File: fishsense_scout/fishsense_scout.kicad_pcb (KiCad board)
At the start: 2 copper layers, 19.5 x 22 mm, 21 parts, among them J1 Conn_01x02_Pin, J2 Conn_01x02_Pin, Q1 NPN, Q2 PMOS, U1 LMR16030PDDA

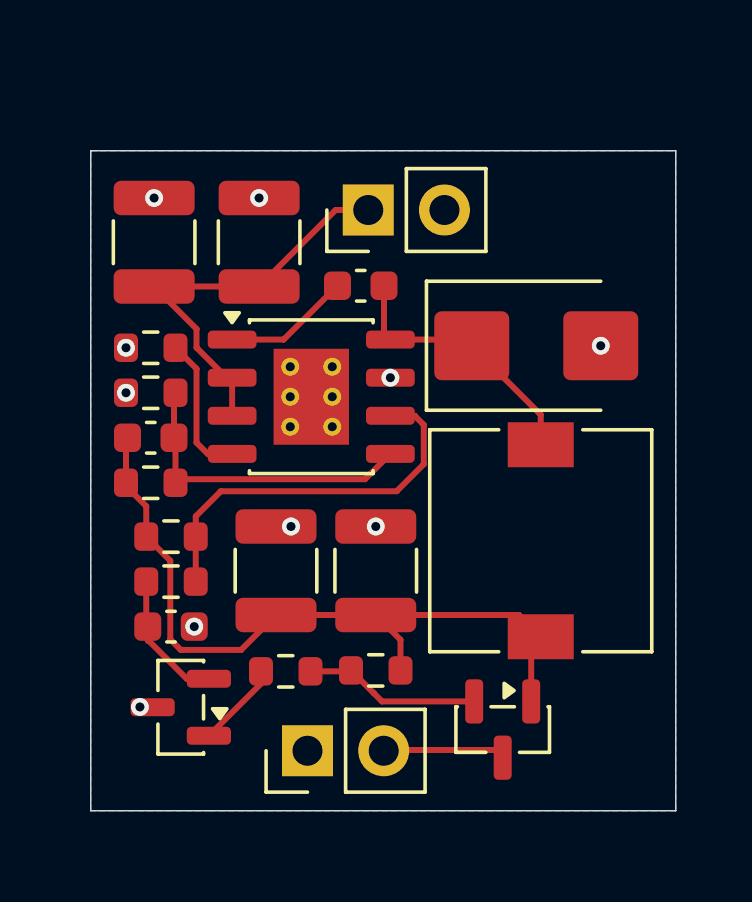
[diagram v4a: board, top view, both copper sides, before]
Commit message: Changed pin headers into screw terminal blocks
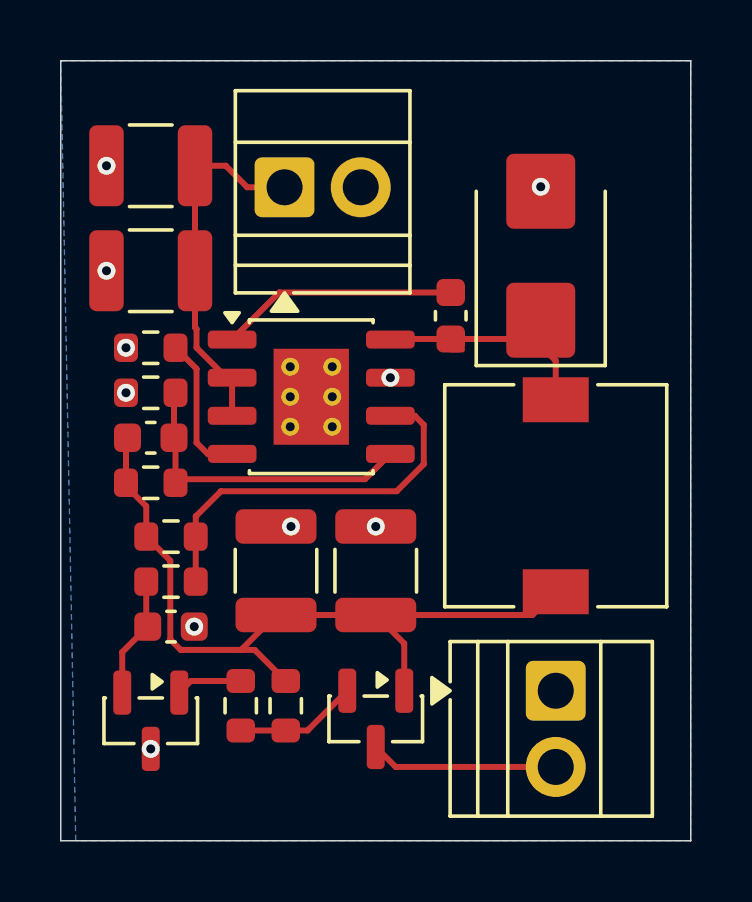
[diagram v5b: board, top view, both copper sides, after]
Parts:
- J1, J2: footprint Connector_PinHeader_2.54mm:PinHeader_1x02_P2.54mm_Vertical -> TerminalBlock:TerminalBlock_Xinya_XY308-2.54-2P_1x02_P2.54mm_Horizontal
- moved J2 8.51 mm to (160.0, 92.5), turned to -90 degrees
- moved Cin2 4.42 mm to (146.5, 75.0), turned to 180 degrees
- moved Q2 4.25 mm to (154.0, 93.4)
- moved Rpmpu1 3.22 mm to (151.0, 93.0), turned to -90 degrees
- moved Cboot1 3.16 mm to (156.5, 80.0), turned to 90 degrees
- moved Dbreak1 3.00 mm to (159.5, 78.0), turned to 90 degrees
- moved J1 2.89 mm to (151.0, 75.7), turned to 0 degrees
- moved Rpmos1 1.89 mm to (149.5, 93.0), turned to 90 degrees
- moved L1 1.58 mm to (160.0, 86.0)
- moved Q1 1.10 mm to (146.5, 93.5), turned to -90 degrees
- moved Cin1 0.96 mm to (146.5, 78.5), turned to 180 degrees
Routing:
- net Net-(U1-BOOT): track 4.85 -> 8.54 mm
- net /Vout: track 3.25 -> 6.28 mm
- net Net-(Q2-G): track 5.93 -> 4.25 mm
- net /Vin: track 14.3 -> 12.9 mm
- net Net-(Q1-B): track 5.17 -> 4.24 mm
- net Net-(Q2-D): track 25.6 -> 26.4 mm
- net Net-(Q1-C): track 2.87 -> 2.21 mm
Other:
- board size 19.5 x 22 mm -> 21 x 26 mm
